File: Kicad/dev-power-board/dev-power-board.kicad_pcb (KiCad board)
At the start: 2 copper layers, 55 x 30 mm, 25 parts, among them J10 Conn_01x02_Male, J11 Conn_02x03_Counter_Clockwise, J12 Conn_01x02_Male, J3 Conn_01x01_Male, J4 Conn_01x01_Male, J5 Conn_02x03_Counter_Clockwise, J6 Conn_01x02_Male, J7 Conn_01x02_Male, J8 Conn_02x03_Counter_Clockwise, J9 Conn_01x02_Male, U1 AMS1117-5.0, U2 AMS1117-3.3

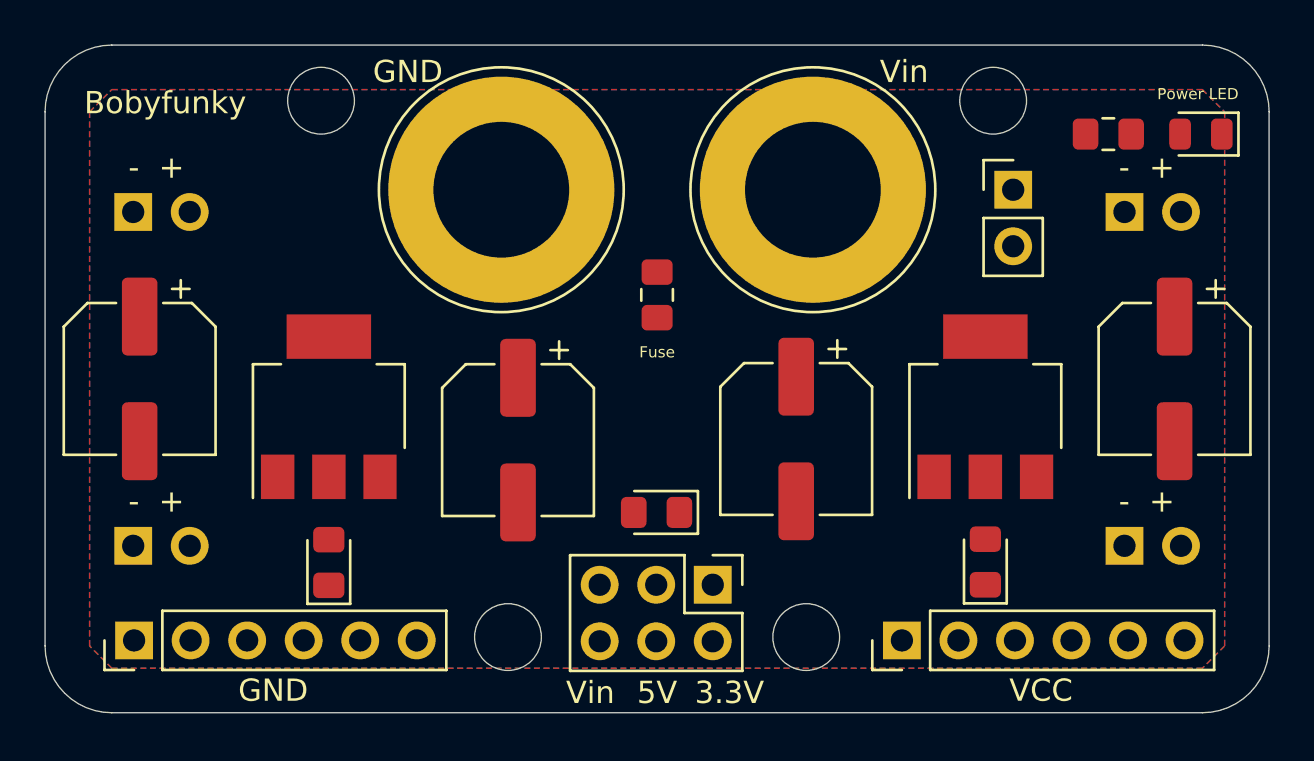
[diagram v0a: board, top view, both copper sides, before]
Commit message: Tracks width + silk
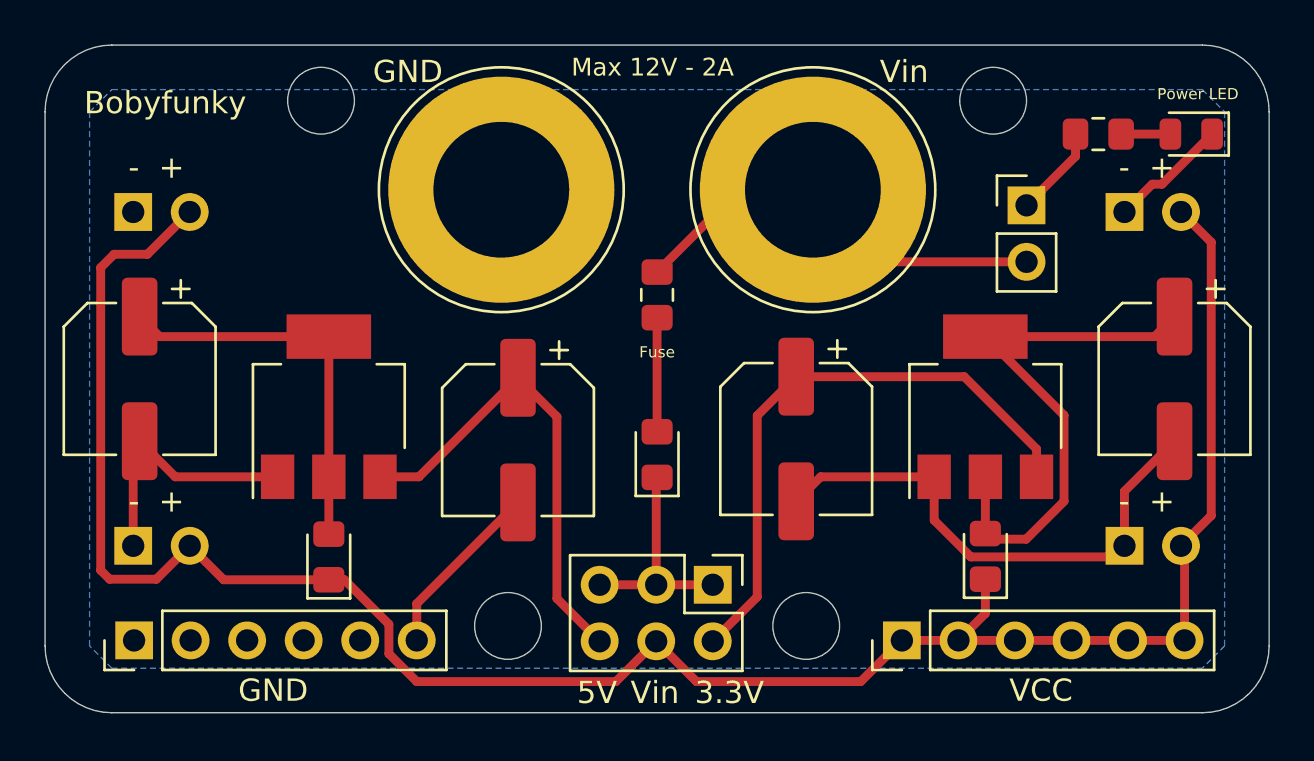
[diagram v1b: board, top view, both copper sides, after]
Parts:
- moved D1 2.60 mm to (130.0, 58.4), turned to 90 degrees
- moved J12 0.92 mm to (146.6, 47.2)
- moved R1 0.45 mm to (149.8, 44.0)
- moved D4 0.44 mm to (154.0, 44.0)
- moved D2 0.25 mm to (115.2, 63.0)
- moved D3 0.25 mm to (144.8, 63.0)
- turned F1 to 270 degrees
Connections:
- D1 pad 1: /pwr_dest -> Net-(D1-Pad1)
- F1 pad 2: Net-(F1-Pad2) -> Net-(D1-Pad2)
- J8 pad 1: Net-(F1-Pad2) -> Net-(D1-Pad1)
- J8 pad 2: Net-(C1-Pad1) -> Net-(C2-Pad1)
- J8 pad 3: Net-(F1-Pad2) -> Net-(D1-Pad1)
- J8 pad 4: Net-(C2-Pad1) -> /pwr_dest
- J8 pad 5: Net-(F1-Pad2) -> Net-(D1-Pad1)
- J8 pad 6: Net-(D1-Pad2) -> Net-(C1-Pad1)
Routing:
- net /pwr_dest: track 0.00 -> 97.1 mm
- net GND: track 0.00 -> 48.8 mm
- net Net-(C2-Pad1): track 0.00 -> 26.8 mm
- net Net-(C4-Pad1): track 0.00 -> 24.8 mm
- net VCC: track 0.00 -> 23.1 mm
- net Net-(C1-Pad1): track 0.00 -> 21.4 mm
- net Net-(C3-Pad1): track 0.00 -> 18.0 mm
- net Net-(D1-Pad1): track 0.00 -> 9.92 mm
- net Net-(D1-Pad2): track 0.00 -> 5.12 mm
- net Net-(J12-Pad1): track 0.00 -> 4.11 mm
- net Net-(D4-Pad2): track 0.00 -> 2.21 mm
- removed copper zone on F.Cu, net VCC
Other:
- outline, holes or cut-outs redrawn
- net class Default: trace_width 0.25 -> 0.4
- net class Vin removed
- board text added: "Max 12V - 2A"

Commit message: Drill holes
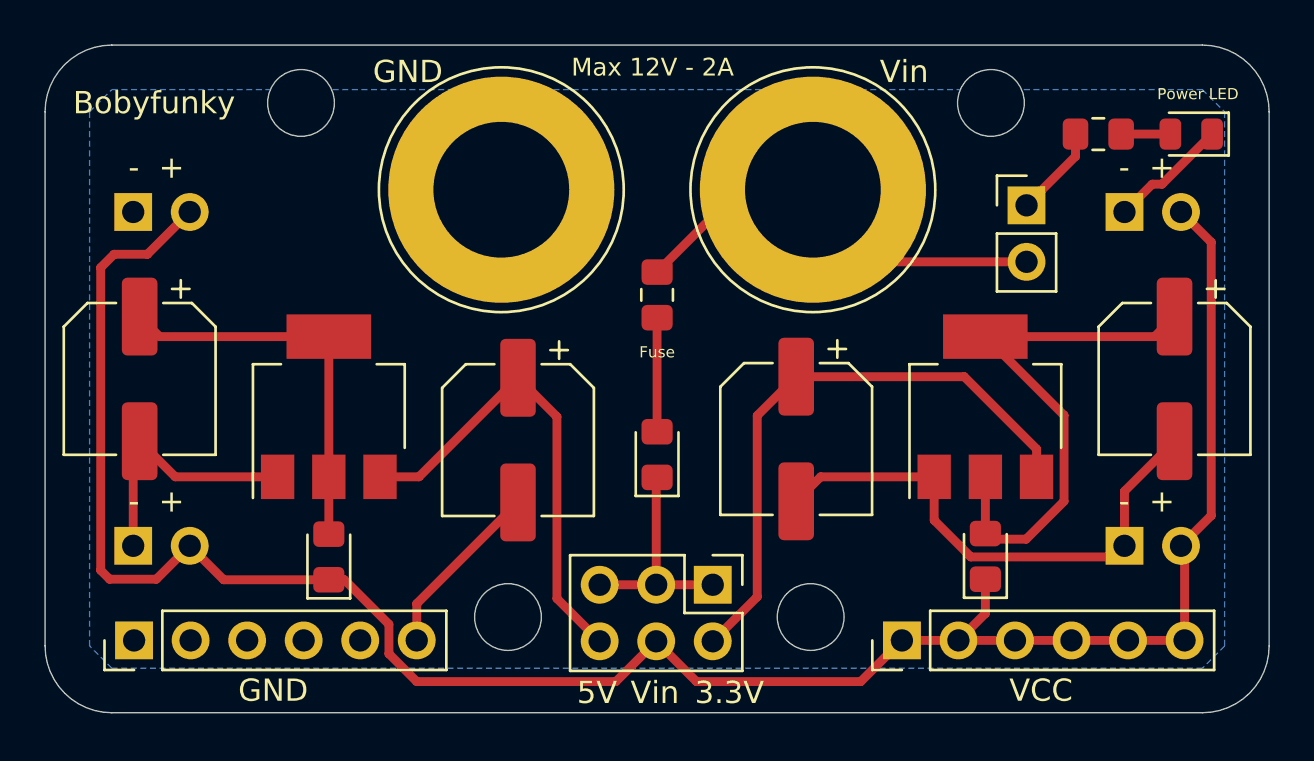
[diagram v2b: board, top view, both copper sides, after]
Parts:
- added REF**: MountingHole_3mm, MountingHole:MountingHole_3mm, F.Cu at (136.9, 65.7)
- added REF**: MountingHole_3mm, MountingHole:MountingHole_3mm, F.Cu at (123.3, 65.7)
- added REF**: MountingHole_3mm, MountingHole:MountingHole_3mm, F.Cu at (114.0, 42.6)
- added REF**: MountingHole_3mm, MountingHole:MountingHole_3mm, F.Cu at (145.0, 42.6)
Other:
- outline, holes or cut-outs redrawn
